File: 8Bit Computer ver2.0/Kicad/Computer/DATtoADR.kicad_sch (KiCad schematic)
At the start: 6 parts, among them IC207 SN74ABT574ADWR, IC208 SN74ABT574ADWR, IC209 SN74LVC1G14DBVR, IC210 SN74AHC74DR, IC211 SN74ABT245BDWR, IC212 SN74ABT245BDWR

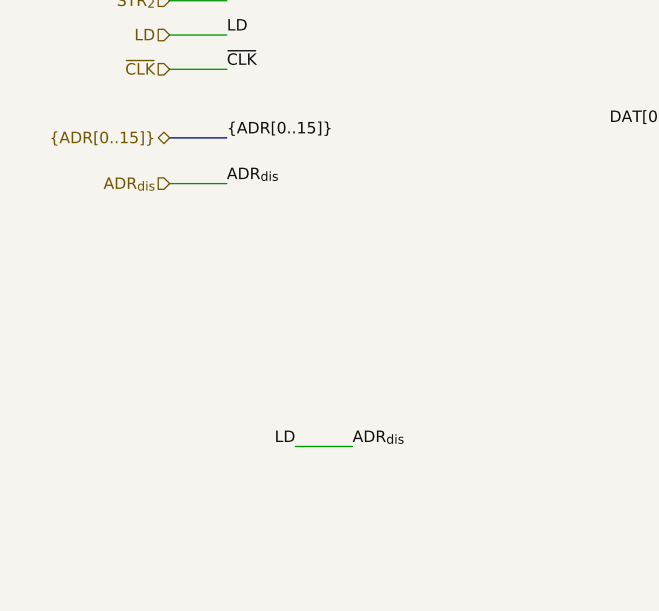
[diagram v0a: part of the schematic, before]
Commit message: Kicad, parts
Parts:
added Leds
Kicad:
added Input Output
changed Q bus to DAT bus
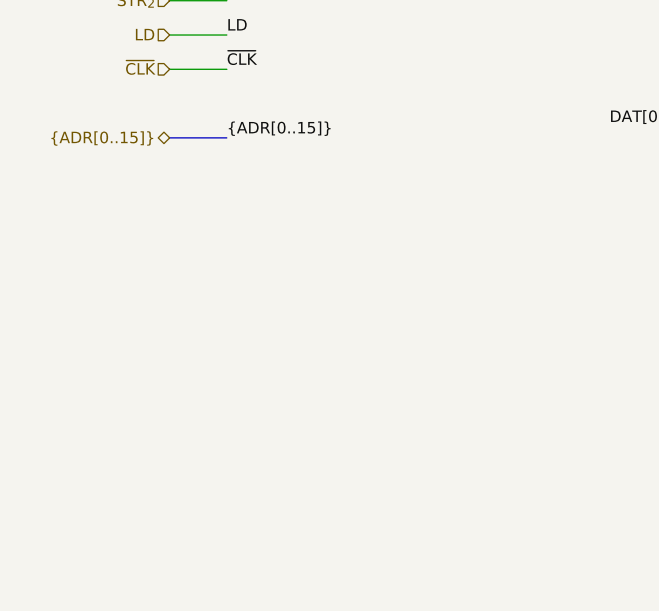
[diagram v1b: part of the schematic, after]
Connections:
- net ADR_{dis} renamed LD
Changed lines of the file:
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@@
-		)
-	)
-	(wire
-		(pts
-			(xy 39.37 80.01) (xy 45.72 80.01)
-		)
-		(stroke
-			(width 0)
-			(type default)
 		)
 	)
@@
 		(pts
 			(xy 134.62 45.72) (xy 187.96 45.72)
-		)
-		(stroke
-			(width 0)
-			(type default)
-		)
-	)
-	(wire
-		(pts
-			(xy 53.34 109.22) (xy 59.69 109.22)
 		)
 		(stroke
@@
 		)
 	)
-	(label "LD"
-		(at 53.34 109.22 180)
-		(effects
-			(font
-				(size 1.27 1.27)
-			)
-			(justify right bottom)
-		)
-	)
 	(label "VCC"
 		(at 185.42 77.47 180)
@@
 	(label "~{CLK}"
 		(at 45.72 67.31 0)
-		(effects
-			(font
-				(size 1.27 1.27)
-			)
-			(justify left bottom)
-		)
-	)
-	(label "ADR_{dis}"
-		(at 59.69 109.22 0)
-		(effects
-			(font
-				(size 1.27 1.27)
-			)
-			(justify left bottom)
-		)
-	)
-	(label "ADR_{dis}"
-		(at 45.72 80.01 0)
 		(effects
 			(font
@@
 		(effects
 			(font
-				(size 1.27 1.27)
-			)
-			(justify right)
-		)
-	)
-	(hierarchical_label "ADR_{dis}"
-		(shape input)
-		(at 39.37 80.01 180)
-		(effects
-			(font

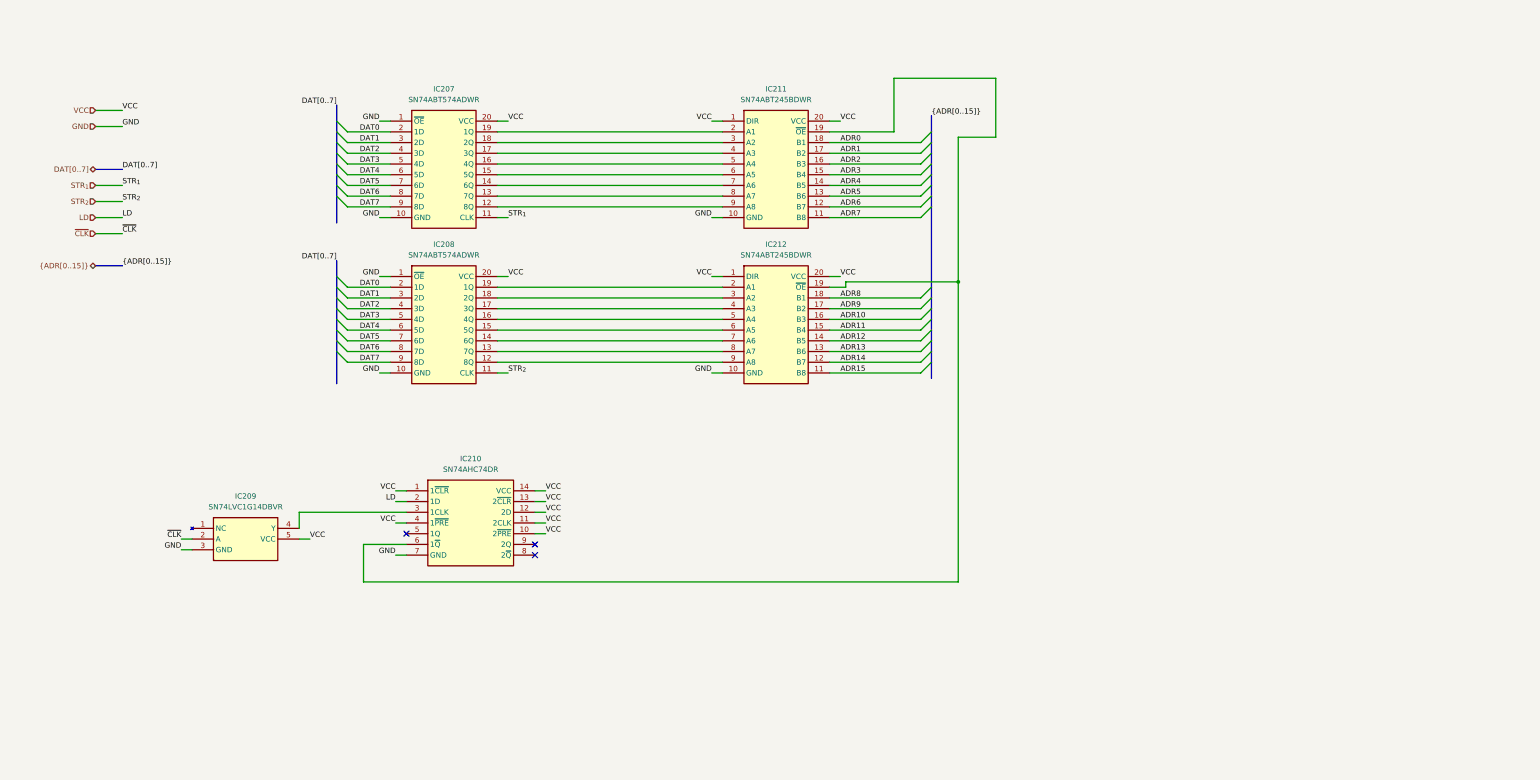
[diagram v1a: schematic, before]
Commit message: Kicad, parts
parts:
added USB C PD Triggerboard
added Delay Chip for 90ns
added Push Button
Kicad:
added USB C PD Triggerboard
added rising edge detector via Delay and Xor for Accept Push Button
added VBUS net
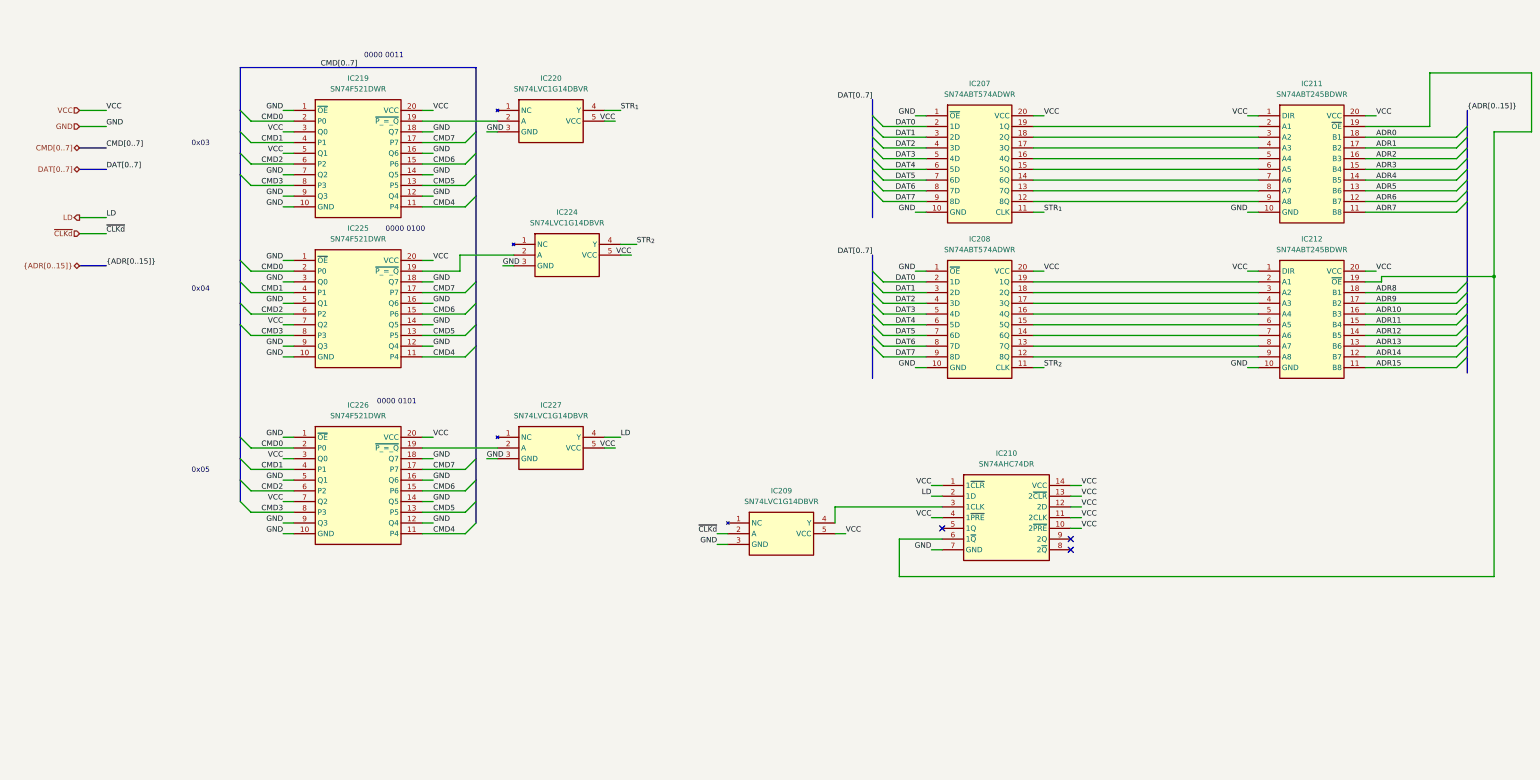
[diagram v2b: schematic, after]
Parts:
- added IC219, IC225, IC226: SN74F521DWR, Samacsys:SOIC127P1030X265-20N, symbol Samacsys:SN74F521DWR
- added IC220, IC224, IC227: SN74LVC1G14DBVR, Samacsys:SOT95P280X145-5N, symbol Samacsys:SN74LVC1G14DBVR
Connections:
- net GND: now also IC219.1 (~{OE}), IC219.10 (GND), IC219.12 (Q4), IC219.14 (Q5), IC219.16 (Q6), IC219.18 (Q7), IC219.7 (Q2), IC219.9 (Q3), IC220.3 (GND), IC224.3 (GND), IC225.1 (~{OE}), IC225.10 (GND), IC225.12 (Q4), IC225.14 (Q5), IC225.16 (Q6), IC225.18 (Q7), IC225.3 (Q0), IC225.5 (Q1), IC225.9 (Q3), IC226.1 (~{OE}), IC226.10 (GND), IC226.12 (Q4), IC226.14 (Q5), IC226.16 (Q6), IC226.18 (Q7), IC226.5 (Q1), IC226.9 (Q3), IC227.3 (GND)
- net LD: now also IC227.4 (Y)
- net STR_{1}: now also IC220.4 (Y)
- net STR_{2}: now also IC224.4 (Y)
- net VCC: now also IC219.20 (VCC), IC219.3 (Q0), IC219.5 (Q1), IC220.5 (VCC), IC224.5 (VCC), IC225.20 (VCC), IC225.7 (Q2), IC226.20 (VCC), IC226.3 (Q0), IC226.7 (Q2), IC227.5 (VCC)
- net ~{CLK} renamed ~{CLKd}
- new net: IC219.19 (~{P_=_Q}), IC220.2 (A)
- new net: IC226.19 (~{P_=_Q}), IC227.2 (A)
- new net: IC224.2 (A), IC225.19 (~{P_=_Q})
- new net CMD0: IC219.2 (P0), IC225.2 (P0), IC226.2 (P0)
- new net CMD1: IC219.4 (P1), IC225.4 (P1), IC226.4 (P1)
- new net CMD2: IC219.6 (P2), IC225.6 (P2), IC226.6 (P2)
- new net CMD3: IC219.8 (P3), IC225.8 (P3), IC226.8 (P3)
- new net CMD4: IC219.11 (P4), IC225.11 (P4), IC226.11 (P4)
- new net CMD5: IC219.13 (P5), IC225.13 (P5), IC226.13 (P5)
- new net CMD6: IC219.15 (P6), IC225.15 (P6), IC226.15 (P6)
- new net CMD7: IC219.17 (P7), IC225.17 (P7), IC226.17 (P7)
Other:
- note added: "0000 0011"
- note added: "0000 0100"
- note added: "0000 0101"
- note added: "0x03"
- note added: "0x04"
- note added: "0x05"
- moved on the sheet: IC207, IC208, IC209, IC210, IC211, IC212

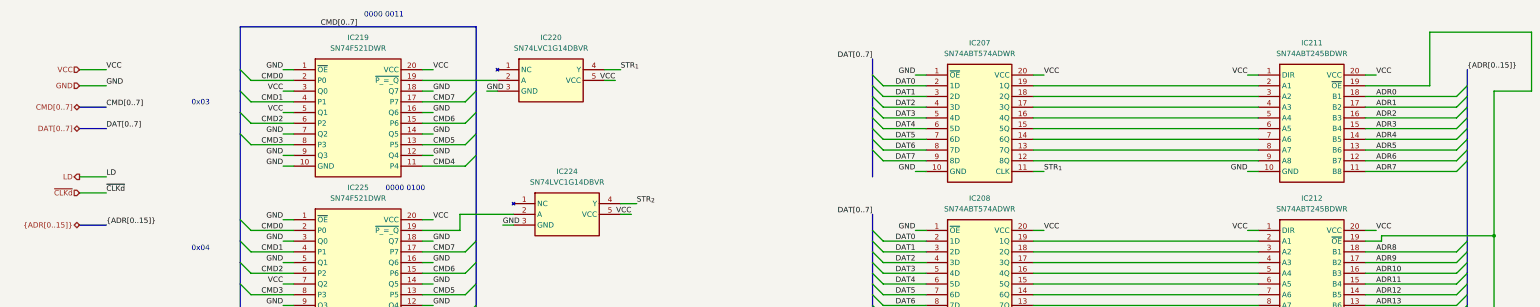
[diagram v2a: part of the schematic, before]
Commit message: Kicad
changed to module version
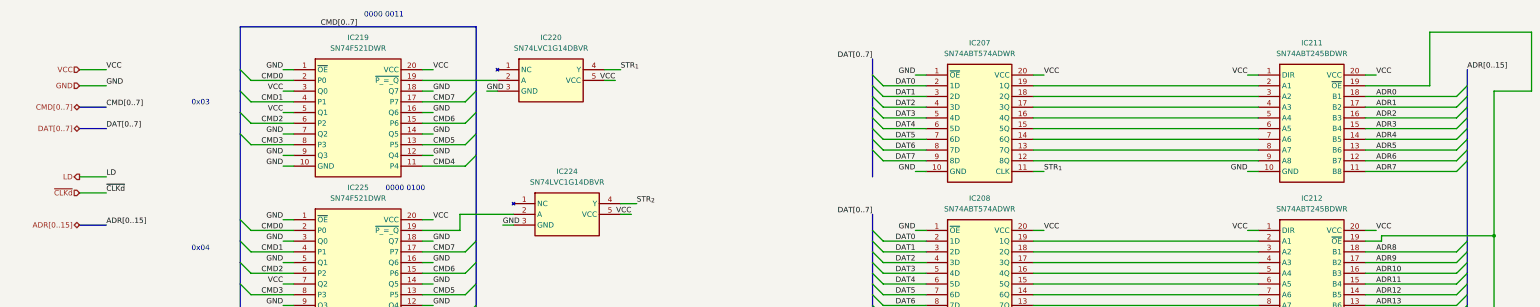
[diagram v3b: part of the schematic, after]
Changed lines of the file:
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@@
 		)
 	)
-	(label "{ADR[0..15]}"
+	(label "ADR[0..15]"
 		(at 364.49 38.1 0)
 		(effects
@@
 		)
 	)
-	(label "{ADR[0..15]}"
+	(label "ADR[0..15]"
 		(at 41.91 74.93 0)
 		(effects
@@
 		)
 	)
-	(hierarchical_label "{ADR[0..15]}"
+	(hierarchical_label "ADR[0..15]"
 		(shape tri_state)
 		(at 35.56 74.93 180)

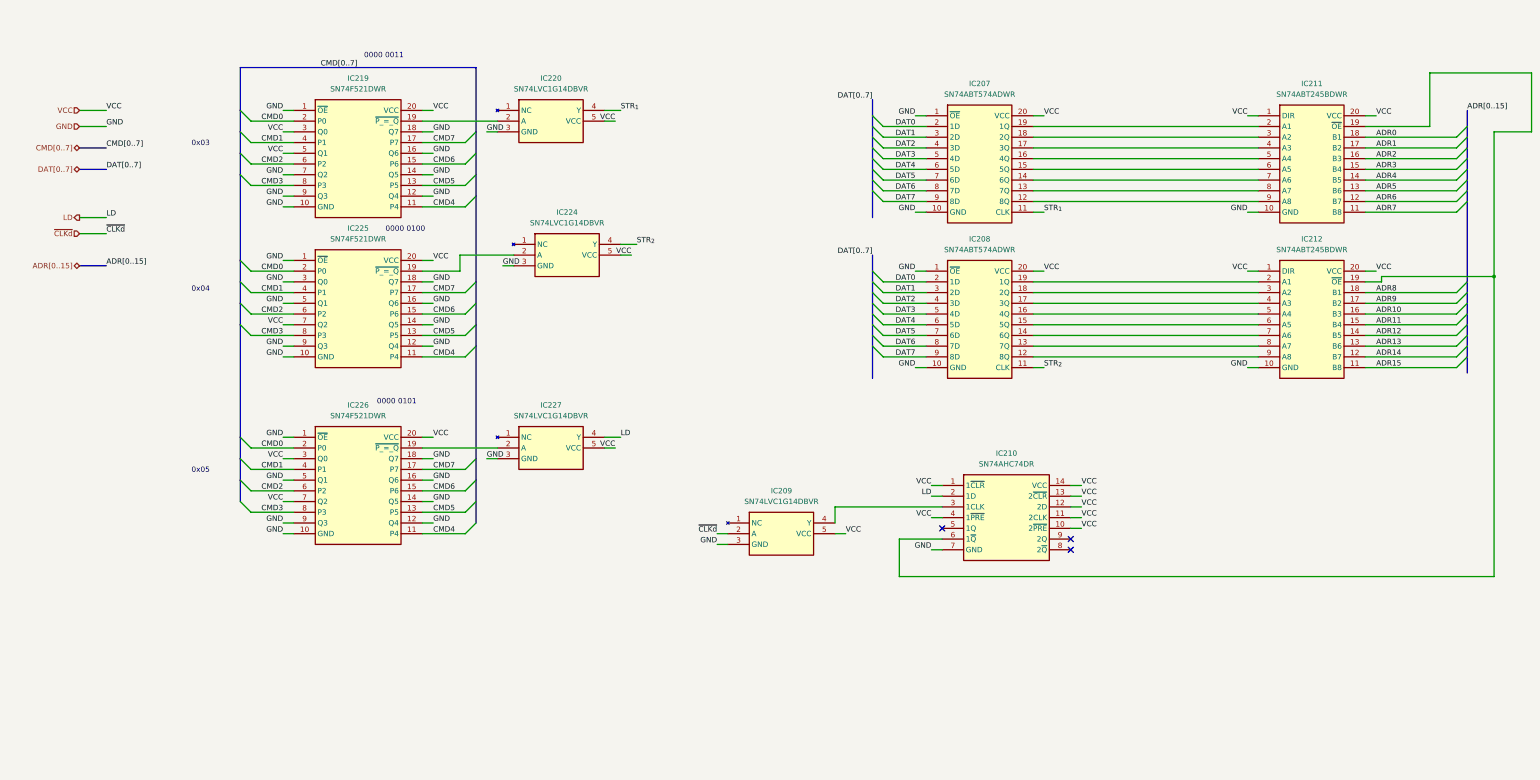
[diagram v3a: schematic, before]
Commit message: Kicad SCH/PCB
Kicad SCH/PCB:
changed the References in SCH
began with INOUTPUT module nearly done
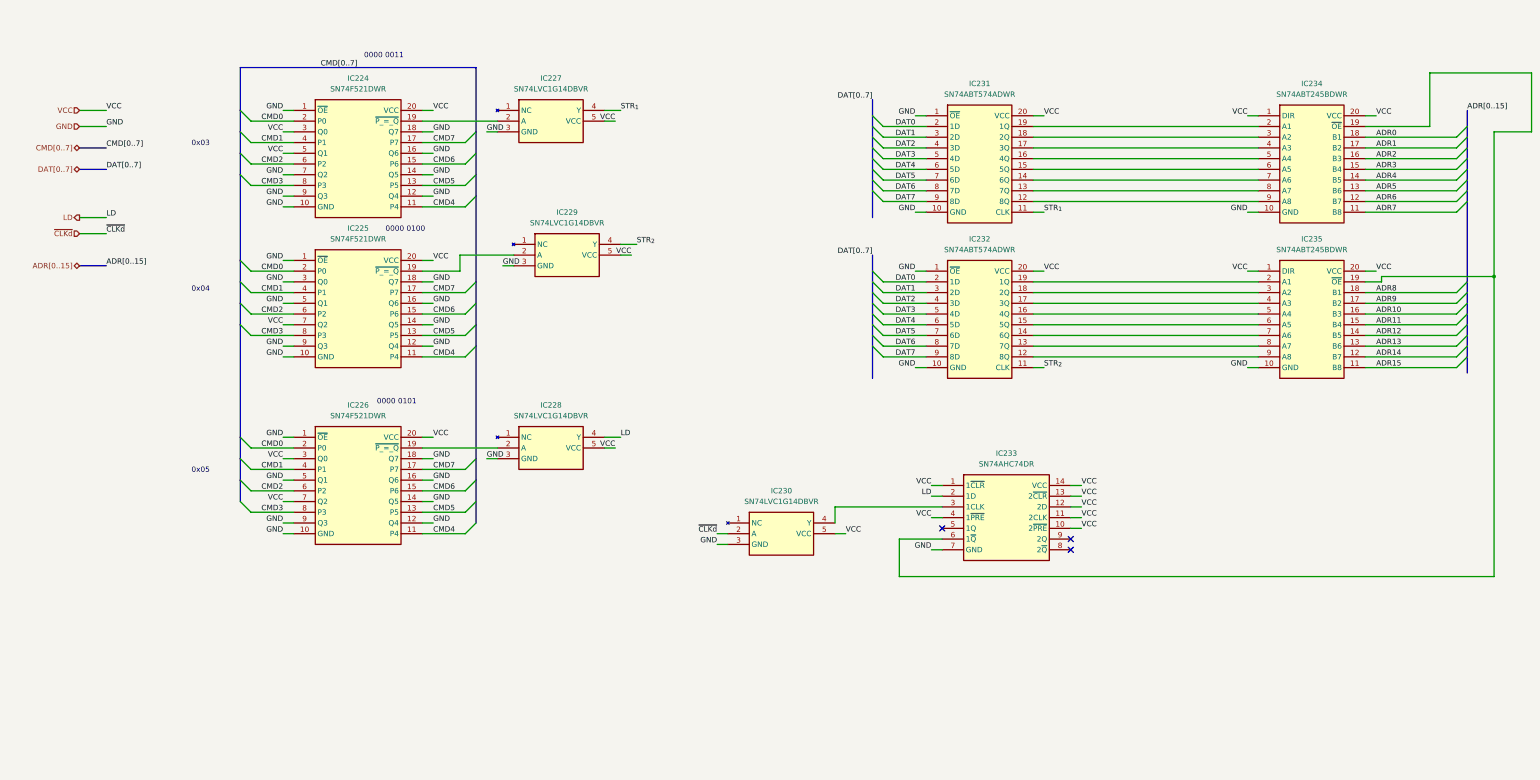
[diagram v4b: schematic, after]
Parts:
- renumbered IC219 to IC224, IC220 to IC227, IC227 to IC228, IC224 to IC229, IC209 to IC230, IC207 to IC231, IC208 to IC232, IC210 to IC233, IC211 to IC234, IC212 to IC235
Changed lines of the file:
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@@
 		(dnp no)
 		(fields_autoplaced yes)
-		(property "Reference" "IC220"
+		(property "Reference" "IC227"
 			(at 147.32 30.48 0)
 			(effects
@@
 			(project "Computer"
 				(path "/1196a00e-6878-4d6d-82b7-9e052dfe7c14/38ef002d-382e-42a8-ab7d-73fd8329d0a3"
-					(reference "IC220")
+					(reference "IC227")
 					(unit 1)
 				)
@@
 		(dnp no)
 		(fields_autoplaced yes)
-		(property "Reference" "IC208"
+		(property "Reference" "IC232"
 			(at 248.92 68.58 0)
 			(effects
@@
 			(project "Computer"
 				(path "/1196a00e-6878-4d6d-82b7-9e052dfe7c14/38ef002d-382e-42a8-ab7d-73fd8329d0a3"
-					(reference "IC208")
+					(reference "IC232")
 					(unit 1)
 				)
@@
 		(dnp no)
 		(fields_autoplaced yes)
-		(property "Reference" "IC210"
+		(property "Reference" "IC233"
 			(at 255.27 119.38 0)
 			(effects
@@
 			(project ""
 				(path "/1196a00e-6878-4d6d-82b7-9e052dfe7c14/38ef002d-382e-42a8-ab7d-73fd8329d0a3"
-					(reference "IC210")
+					(reference "IC233")
 					(unit 1)
 				)
@@
 		(dnp no)
 		(fields_autoplaced yes)
-		(property "Reference" "IC212"
+		(property "Reference" "IC235"
 			(at 327.66 68.58 0)
 			(effects
@@
 			(project "Computer"
 				(path "/1196a00e-6878-4d6d-82b7-9e052dfe7c14/38ef002d-382e-42a8-ab7d-73fd8329d0a3"
-					(reference "IC212")
+					(reference "IC235")
 					(unit 1)
 				)
@@
 		(dnp no)
 		(fields_autoplaced yes)
-		(property "Reference" "IC211"
+		(property "Reference" "IC234"
 			(at 327.66 31.75 0)
 			(effects
@@
 			(project ""
 				(path "/1196a00e-6878-4d6d-82b7-9e052dfe7c14/38ef002d-382e-42a8-ab7d-73fd8329d0a3"
-					(reference "IC211")
+					(reference "IC234")
 					(unit 1)
 				)
@@
 		(dnp no)
 		(fields_autoplaced yes)
-		(property "Reference" "IC209"
+		(property "Reference" "IC230"
 			(at 201.93 128.27 0)
 			(effects
@@
 			(project ""
 				(path "/1196a00e-6878-4d6d-82b7-9e052dfe7c14/38ef002d-382e-42a8-ab7d-73fd8329d0a3"
-					(reference "IC209")
+					(reference "IC230")
 					(unit 1)
 				)
@@
 		(dnp no)
 		(fields_autoplaced yes)
-		(property "Reference" "IC219"
+		(property "Reference" "IC224"
 			(at 101.6 30.48 0)
 			(effects
@@
 			(project "Computer"
 				(path "/1196a00e-6878-4d6d-82b7-9e052dfe7c14/38ef002d-382e-42a8-ab7d-73fd8329d0a3"
-					(reference "IC219")
+					(reference "IC224")
 					(unit 1)
 				)
@@
 		(dnp no)
 		(fields_autoplaced yes)
-		(property "Reference" "IC207"
+		(property "Reference" "IC231"
 			(at 248.92 31.75 0)
 			(effects
@@
 			(project ""
 				(path "/1196a00e-6878-4d6d-82b7-9e052dfe7c14/38ef002d-382e-42a8-ab7d-73fd8329d0a3"
-					(reference "IC207")
+					(reference "IC231")
 					(unit 1)
 				)
@@
 		(dnp no)
 		(fields_autoplaced yes)
-		(property "Reference" "IC227"
+		(property "Reference" "IC228"
 			(at 147.32 107.95 0)
 			(effects
@@
 			(project "Computer"
 				(path "/1196a00e-6878-4d6d-82b7-9e052dfe7c14/38ef002d-382e-42a8-ab7d-73fd8329d0a3"
-					(reference "IC227")
+					(reference "IC228")
 					(unit 1)
 				)
@@
 		(dnp no)
 		(fields_autoplaced yes)
-		(property "Reference" "IC224"
+		(property "Reference" "IC229"
 			(at 151.13 62.23 0)
 			(effects
@@
 			(project "Computer"
 				(path "/1196a00e-6878-4d6d-82b7-9e052dfe7c14/38ef002d-382e-42a8-ab7d-73fd8329d0a3"
-					(reference "IC224")
+					(reference "IC229")
 					(unit 1)
 				)
